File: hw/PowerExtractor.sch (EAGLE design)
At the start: 84 parts, among them IC1 LM358D, Q1 BSS84, Q3 BC847SMD, Q4 BC847SMD, Q5 BC847SMD, Q6 BC847SMD, T1 IRL530N, T2 IRF7416, T3 IRLL014N_, T4 IRLL014N_, U1 ZXCT1086E5TA, U2 ZXCT1086E5TA

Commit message: Completely routed
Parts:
- removed OPH1: VT90N1, photo-elements:VT90N1
- removed T3, T4: IRLL014N_, triakcz:IRLL014N_
- added PHOTORESIST: (no value), pinhead:PINHD-1X2
- added Q2: IRL530, transistor-power:IRF530
- added Q7: IRF530, transistor-power:IRF530
- R18, R19, R21, R7: device rcl:R-EU_0207/10 -> rcl:R-EU_M0805
- R23: device rcl:R-EU_0207/10 -> rcl:R-EU_R0805
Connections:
- net ARDUINO_LIGHT_IN: now also PHOTORESIST.2; no longer OPH1.1
- net GND: now also PHOTORESIST.1, Q2.S, Q7.S; no longer OPH1.2, T3.S, T4.S
- net N$24: now also Q2.G; no longer T3.G
- net N$25: now also Q2.D; no longer T3.D
- net N$27: now also Q7.G; no longer T4.G
- net N$28: now also Q7.D; no longer T4.D
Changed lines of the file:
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@@
 <part name="R11" library="rcl" deviceset="R-EU_" device="0207/10" value="100k"/>
 <part name="R12" library="rcl" deviceset="R-EU_" device="0207/10" value="47k"/>
-<part name="OPH1" library="photo-elements" deviceset="VT9" device="" technology="0N1"/>
 <part name="R13" library="rcl" deviceset="R-EU_" device="M1206" value="0R01"/>
 <part name="U1" library="triakcz" deviceset="ZXCT1086E5TA" device=""/>
@@
 <part name="Q4" library="triakcz" deviceset="BC847*" device="SMD"/>
 <part name="R17" library="rcl" deviceset="R-EU_" device="0207/10" value="100k"/>
-<part name="R18" library="rcl" deviceset="R-EU_" device="0207/10" value="100k"/>
+<part name="R18" library="rcl" deviceset="R-EU_" device="M0805" value="100k"/>
 <part name="D5" library="diode" deviceset="ZENER-DIODE" device="SOD80C" value="BZV55C15SMD"/>
-<part name="R7" library="rcl" deviceset="R-EU_" device="0207/10" value="220R"/>
-<part name="R19" library="rcl" deviceset="R-EU_" device="0207/10" value="330k"/>
+<part name="R7" library="rcl" deviceset="R-EU_" device="M0805" value="220R"/>
+<part name="R19" library="rcl" deviceset="R-EU_" device="M0805" value="330k"/>
 <part name="C6" library="rcl" deviceset="C-EU" device="C0805" value="100n"/>
 <part name="D7" library="triakcz" deviceset="1N4148" device="MINIMELF"/>
@@
 <part name="HEAD_LED" library="con-wago-500" deviceset="W237-102" device=""/>
 <part name="C8" library="rcl" deviceset="C-EU" device="C0805" value="100n"/>
-<part name="T3" library="triakcz" deviceset="IRLL014N" device="_"/>
 <part name="R20" library="rcl" deviceset="R-EU_" device="0207/10" value="2k2"/>
-<part name="R21" library="rcl" deviceset="R-EU_" device="0207/10" value="100k"/>
+<part name="R21" library="rcl" deviceset="R-EU_" device="M0805" value="100k"/>
 <part name="TAIL_LED" library="con-wago-500" deviceset="W237-102" device=""/>
-<part name="T4" library="triakcz" deviceset="IRLL014N" device="_"/>
 <part name="R22" library="rcl" deviceset="R-EU_" device="0207/10" value="2k2"/>
-<part name="R23" library="rcl" deviceset="R-EU_" device="0207/10" value="100k"/>
+<part name="R23" library="rcl" deviceset="R-EU_" device="R0805" value="100k"/>
 <part name="12VOUT" library="con-wago-500" deviceset="W237-102" device=""/>
 <part name="F3" library="fuse" deviceset="SHK20L" device="" value="F1.5A"/>
@@
 <part name="D10" library="triakcz" deviceset="1N4148" device="MINIMELF"/>
 <part name="C14" library="rcl" deviceset="C-EU" device="C0805" value="1uF/50V"/>
+<part name="Q2" library="transistor-power" deviceset="IRF530" device="" value="IRL530"/>
+<part name="Q7" library="transistor-power" deviceset="IRF530" device="" value="IRF530"/>
+<part name="PHOTORESIST" library="pinhead" deviceset="PINHD-1X2" device=""/>
 </parts>
 <sheets>
@@
 <instance part="R11" gate="G$1" x="185.42" y="48.26" rot="R90"/>
 <instance part="R12" gate="G$1" x="-12.7" y="200.66" rot="R180"/>
-<instance part="OPH1" gate="G$1" x="17.78" y="200.66" rot="R90"/>
 <instance part="R13" gate="G$1" x="198.12" y="86.36"/>
 <instance part="U1" gate="A" x="248.92" y="119.38"/>
@@
 <instance part="HEAD_LED" gate="-2" x="556.26" y="45.72" rot="R180"/>
 <instance part="C8" gate="G$1" x="520.7" y="33.02" rot="R180"/>
-<instance part="T3" gate="A" x="589.28" y="33.02"/>
 <instance part="R20" gate="G$1" x="581.66" y="38.1" rot="R90"/>
 <instance part="R21" gate="G$1" x="581.66" y="25.4" rot="R270"/>
 <instance part="TAIL_LED" gate="-1" x="604.52" y="50.8" rot="R180"/>
 <instance part="TAIL_LED" gate="-2" x="604.52" y="55.88" rot="R180"/>
-<instance part="T4" gate="A" x="629.92" y="33.02"/>
 <instance part="R22" gate="G$1" x="622.3" y="38.1" rot="R90"/>
 <instance part="R23" gate="G$1" x="622.3" y="25.4" rot="R270"/>
@@
 <instance part="D10" gate="G$1" x="116.84" y="233.68" rot="R270"/>
 <instance part="C14" gate="G$1" x="40.64" y="223.52"/>
+<instance part="Q2" gate="G$1" x="586.74" y="33.02"/>
+<instance part="Q7" gate="G$1" x="627.38" y="33.02"/>
+<instance part="PHOTORESIST" gate="G$1" x="15.24" y="193.04" rot="R270"/>
 </instances>
 <busses>
@@
 <wire x1="525.78" y1="20.32" x2="581.66" y2="20.32" width="0.1524" layer="91"/>
 <junction x="525.78" y="20.32"/>
-<pinref part="T3" gate="A" pin="S"/>
 <wire x1="581.66" y1="20.32" x2="589.28" y2="20.32" width="0.1524" layer="91"/>
 <wire x1="589.28" y1="20.32" x2="589.28" y2="27.94" width="0.1524" layer="91"/>
@@
 <junction x="231.14" y="101.6"/>
 <wire x1="589.28" y1="20.32" x2="622.3" y2="20.32" width="0.1524" layer="91"/>
-<pinref part="T4" gate="A" pin="S"/>
 <wire x1="622.3" y1="20.32" x2="629.92" y2="20.32" width="0.1524" layer="91"/>
 <wire x1="629.92" y1="20.32" x2="629.92" y2="27.94" width="0.1524" layer="91"/>
@@
 <wire x1="139.7" y1="264.16" x2="68.58" y2="264.16" width="0.1524" layer="91"/>
 <junction x="68.58" y="264.16"/>
-<pinref part="OPH1" gate="G$1" pin="2"/>
-<wire x1="22.86" y1="200.66" x2="27.94" y2="200.66" width="0.1524" layer="91"/>
 <wire x1="27.94" y1="200.66" x2="27.94" y2="20.32" width="0.1524" layer="91"/>
 <junction x="40.64" y="218.44"/>
@@
 <junction x="55.88" y="20.32"/>
 <pinref part="C14" gate="G$1" pin="2"/>
+<pinref part="Q2" gate="G$1" pin="S"/>
+<pinref part="Q7" gate="G$1" pin="S"/>
+<pinref part="PHOTORESIST" gate="G$1" pin="1"/>
+<wire x1="27.94" y1="200.66" x2="17.78" y2="200.66" width="0.1524" layer="91"/>
+<wire x1="17.78" y1="200.66" x2="17.78" y2="195.58" width="0.1524" layer="91"/>
 </segment>
 </net>
@@
 <net name="ARDUINO_LIGHT_IN" class="0">
 <segment>
-<pinref part="OPH1" gate="G$1" pin="1"/>
 <wire x1="-7.62" y1="200.66" x2="2.54" y2="200.66" width="0.1524" layer="91"/>
 <pinref part="R12" gate="G$1" pin="1"/>
-<wire x1="2.54" y1="200.66" x2="12.7" y2="200.66" width="0.1524" layer="91"/>
+<wire x1="2.54" y1="200.66" x2="15.24" y2="200.66" width="0.1524" layer="91"/>
 <wire x1="2.54" y1="200.66" x2="2.54" y2="208.28" width="0.1524" layer="91"/>
 <junction x="2.54" y="200.66"/>
@@
 <wire x1="2.54" y1="208.28" x2="73.66" y2="208.28" width="0.1524" layer="91"/>
 <pinref part="A1" gate="G$1" pin="A0"/>
+<pinref part="PHOTORESIST" gate="G$1" pin="2"/>
+<wire x1="15.24" y1="195.58" x2="15.24" y2="200.66" width="0.1524" layer="91"/>
 </segment>
 </net>
@@
 <net name="N$24" class="0">
 <segment>
-<pinref part="T3" gate="A" pin="G"/>
 <pinref part="R20" gate="G$1" pin="1"/>
 <pinref part="R21" gate="G$1" pin="1"/>
@@
 <junction x="581.66" y="30.48"/>
 <wire x1="581.66" y1="30.48" x2="584.2" y2="30.48" width="0.1524" layer="91"/>
+<pinref part="Q2" gate="G$1" pin="G"/>
 </segment>
 </net>
@@
 <net name="N$25" class="0">
 <segment>
-<pinref part="T3" gate="A" pin="D"/>
 <wire x1="589.28" y1="38.1" x2="589.28" y2="50.8" width="0.1524" layer="91"/>
 <wire x1="589.28" y1="50.8" x2="599.44" y2="50.8" width="0.1524" layer="91"/>
 <pinref part="TAIL_LED" gate="-1" pin="KL"/>
+<pinref part="Q2" gate="G$1" pin="D"/>
 </segment>
 </net>
@@
 <net name="N$27" class="0">
 <segment>
-<pinref part="T4" gate="A" pin="G"/>
 <pinref part="R22" gate="G$1" pin="1"/>
 <pinref part="R23" gate="G$1" pin="1"/>
@@
 <junction x="622.3" y="30.48"/>
 <wire x1="622.3" y1="30.48" x2="624.84" y2="30.48" width="0.1524" layer="91"/>
+<pinref part="Q7" gate="G$1" pin="G"/>
 </segment>
 </net>
@@
 <net name="N$28" class="0">
 <segment>
-<pinref part="T4" gate="A" pin="D"/>
 <wire x1="629.92" y1="38.1" x2="629.92" y2="99.06" width="0.1524" layer="91"/>
 <wire x1="629.92" y1="99.06" x2="665.48" y2="99.06" width="0.1524" layer="91"/>
 <pinref part="12VOUT" gate="-1" pin="KL"/>
-</segment>
-</net>
+<pinref part="Q7" gate="G$1" pin="D"/>
+</segment>
+</net>

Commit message: Fixed speed sense circuit
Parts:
- removed Q3, Q5, Q6: BC847SMD, triakcz:BC847SMD
- removed R27: 470R, rcl:R-EU_R0805
- added D11, D12: 1N4148MINIMELF, triakcz:1N4148MINIMELF
- added R8: 100k, rcl:R-EU_M0805
- added U$2, U$3, U$4: BCV47, triakcz:BCV47
- D10, D9: value 1N4148MINIMELF -> 1N4148DO35-10; device triakcz:1N4148MINIMELF -> triakcz:1N4148DO35-10
- R10: device rcl:R-EU_M0805 -> rcl:R-EU_R0805
- R25: value 330k -> 330K
- R26: value 470R -> 100k; device rcl:R-EU_0207/10 -> rcl:R-EU_M0805
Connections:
- new net N$38: D11.A, R25.1
- new net N$39: A1.D12(MISO), D12.A
- net ARDUINO_ROTATION_INT: now also R26.1, U$2.C; no longer Q6.C
- net ARDUINO_SELF_POWER_OUT: now also D2.A; no longer R11.2
- net GND: now also U$2.E, U$3.E, U$4.E; no longer D9.A, Q3.E, R25.1, R26.1
- net HUB2: now also R25.2
- net N$12: now also D2.C, R11.2; no longer D2.A, R11.1
- net N$22: now also D10.A, R3.1, R6.2, U$4.C; no longer A1.D4, D10.C
- net N$29: now also D9.A; no longer D9.C, Q5.B, R25.2
- net N$30: now also R8.2, U$3.C; no longer Q5.C, R27.1
- net N$31: now also D9.C, U$3.B; no longer Q5.E, Q6.E
- net N$32: now also D11.C, R8.1, U$2.B; no longer Q6.B, R27.2
- net N$36: now also D10.C, D12.C; no longer A1.D12(MISO)
- net N$4: now also R11.1, U$4.B; no longer D2.C, Q3.B
- net N$6: now also A1.D4; no longer D10.A, Q3.C, R3.1, R6.2
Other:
- moved on the sheet: D10, D2, D9, DIRECT_CHARGE-1, DIRECT_CHARGE-2, DISPLAY, DYNAMO-1, DYNAMO-2, KEYBOARD1, R10, R11, R24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

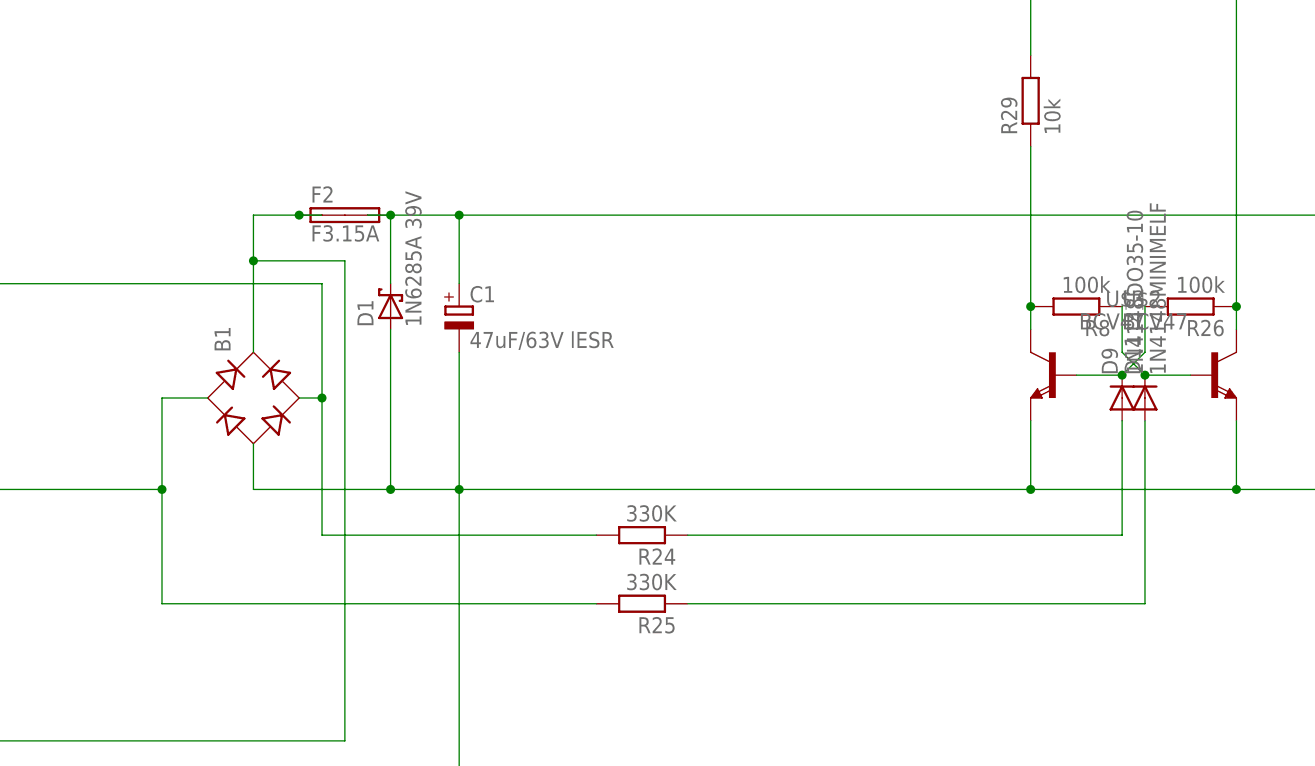
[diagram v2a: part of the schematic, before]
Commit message: Shifted speed sense circuit under MCU
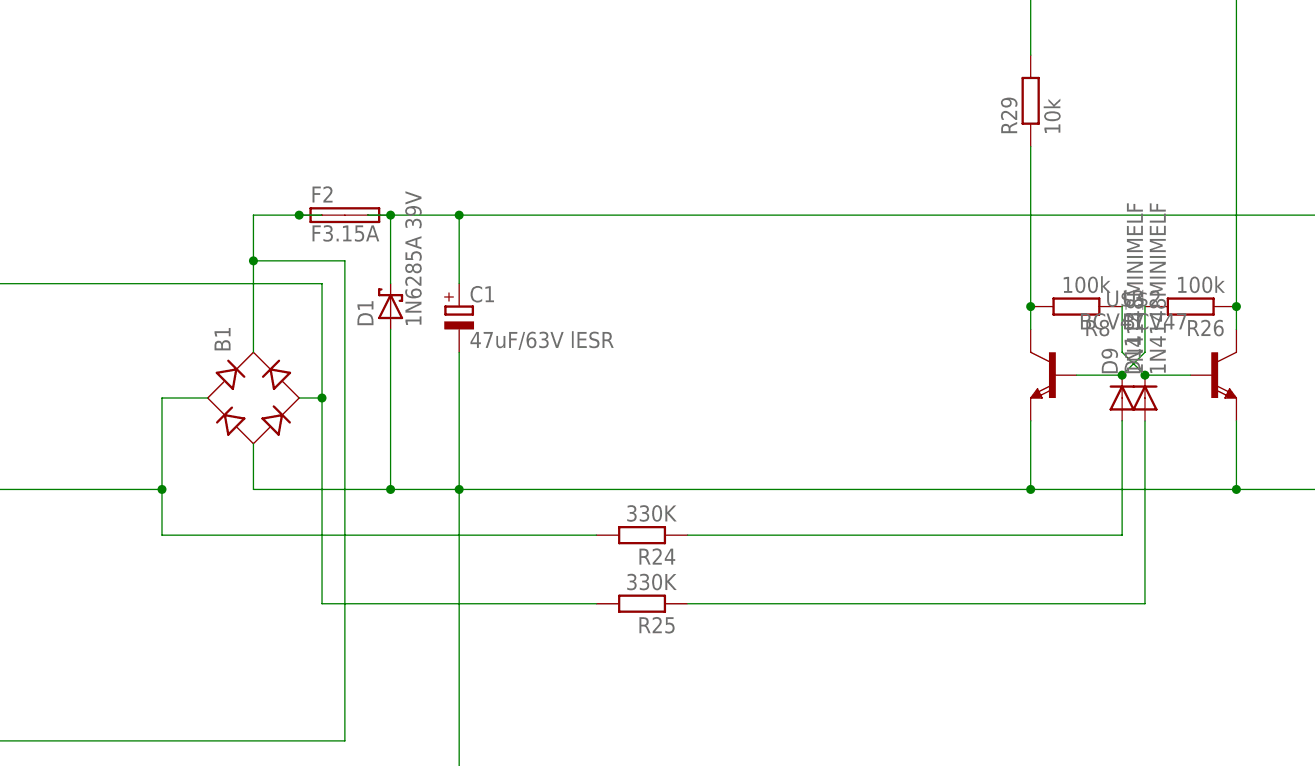
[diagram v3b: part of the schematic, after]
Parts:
- D9: value 1N4148DO35-10 -> 1N4148MINIMELF; device triakcz:1N4148DO35-10 -> triakcz:1N4148MINIMELF
- R26: device rcl:R-EU_M0805 -> rcl:R-EU_R0805
- R8: device rcl:R-EU_M0805 -> rcl:R-EU_0207/10
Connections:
- removed net HUB_1: B1.AC2, DYNAMO-1.KL, R24.2
- new net HUB1: B1.AC2, DYNAMO-1.KL, R25.2
- net HUB2: now also R24.2; no longer R25.2
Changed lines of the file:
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@@
 <part name="F3" library="fuse" deviceset="SHK20L" device="" value="F1.5A"/>
 <part name="R24" library="rcl" deviceset="R-EU_" device="M0805" value="330K"/>
-<part name="D9" library="triakcz" deviceset="1N4148" device="DO35-10" value="1N4148DO35-10"/>
+<part name="D9" library="triakcz" deviceset="1N4148" device="MINIMELF" value="1N4148MINIMELF"/>
 <part name="R28" library="rcl" deviceset="R-EU_" device="R0805" value="10k"/>
 <part name="R29" library="rcl" deviceset="R-EU_" device="M0805" value="10k"/>
@@
 <part name="U$2" library="triakcz" deviceset="BCV47" device=""/>
 <part name="U$3" library="triakcz" deviceset="BCV47" device=""/>
-<part name="R8" library="rcl" deviceset="R-EU_" device="M0805" value="100k"/>
-<part name="R26" library="rcl" deviceset="R-EU_" device="M0805" value="100k"/>
+<part name="R8" library="rcl" deviceset="R-EU_" device="0207/10" value="100k"/>
+<part name="R26" library="rcl" deviceset="R-EU_" device="R0805" value="100k"/>
 <part name="D11" library="triakcz" deviceset="1N4148" device="MINIMELF"/>
 <part name="R25" library="rcl" deviceset="R-EU_" device="M0805" value="330K"/>
@@
 </busses>
 <nets>
-<net name="HUB_1" class="0">
+<net name="HUB1" class="0">
 <segment>
 <wire x1="-127" y1="43.18" x2="-86.36" y2="43.18" width="0.1524" layer="91"/>
@@
 <wire x1="-86.36" y1="30.48" x2="-88.9" y2="30.48" width="0.1524" layer="91"/>
 <pinref part="DYNAMO" gate="-1" pin="KL"/>
+<pinref part="R25" gate="G$1" pin="2"/>
+<wire x1="-55.88" y1="7.62" x2="-86.36" y2="7.62" width="0.1524" layer="91"/>
+<wire x1="-86.36" y1="30.48" x2="-86.36" y2="7.62" width="0.1524" layer="91"/>
 <junction x="-86.36" y="30.48"/>
-<pinref part="R24" gate="G$1" pin="2"/>
-<wire x1="-86.36" y1="30.48" x2="-86.36" y2="15.24" width="0.1524" layer="91"/>
-<wire x1="-86.36" y1="15.24" x2="-55.88" y2="15.24" width="0.1524" layer="91"/>
-</segment>
-</net>
-<net name="HUB2" class="0">
-<segment>
-<pinref part="B1" gate="1" pin="AC1"/>
-<wire x1="-99.06" y1="30.48" x2="-104.14" y2="30.48" width="0.1524" layer="91"/>
-<wire x1="-104.14" y1="30.48" x2="-104.14" y2="20.32" width="0.1524" layer="91"/>
-<pinref part="DYNAMO" gate="-2" pin="KL"/>
-<wire x1="-127" y1="20.32" x2="-104.14" y2="20.32" width="0.1524" layer="91"/>
-<pinref part="R25" gate="G$1" pin="2"/>
-<wire x1="-55.88" y1="7.62" x2="-104.14" y2="7.62" width="0.1524" layer="91"/>
-<wire x1="-104.14" y1="7.62" x2="-104.14" y2="20.32" width="0.1524" layer="91"/>
-<junction x="-104.14" y="20.32"/>
 </segment>
 </net>
@@
 </segment>
 </net>
+<net name="HUB2" class="0">
+<segment>
+<pinref part="DYNAMO" gate="-2" pin="KL"/>
+<wire x1="-127" y1="20.32" x2="-104.14" y2="20.32" width="0.1524" layer="91"/>
+<wire x1="-104.14" y1="30.48" x2="-104.14" y2="20.32" width="0.1524" layer="91"/>
+<pinref part="B1" gate="1" pin="AC1"/>
+<wire x1="-99.06" y1="30.48" x2="-104.14" y2="30.48" width="0.1524" layer="91"/>
+<pinref part="R24" gate="G$1" pin="2"/>
+<wire x1="-104.14" y1="15.24" x2="-55.88" y2="15.24" width="0.1524" layer="91"/>
+<wire x1="-104.14" y1="20.32" x2="-104.14" y2="15.24" width="0.1524" layer="91"/>
+<junction x="-104.14" y="20.32"/>
+</segment>
+</net>
